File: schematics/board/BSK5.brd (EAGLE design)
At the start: 94 x 94 mm, 26 parts

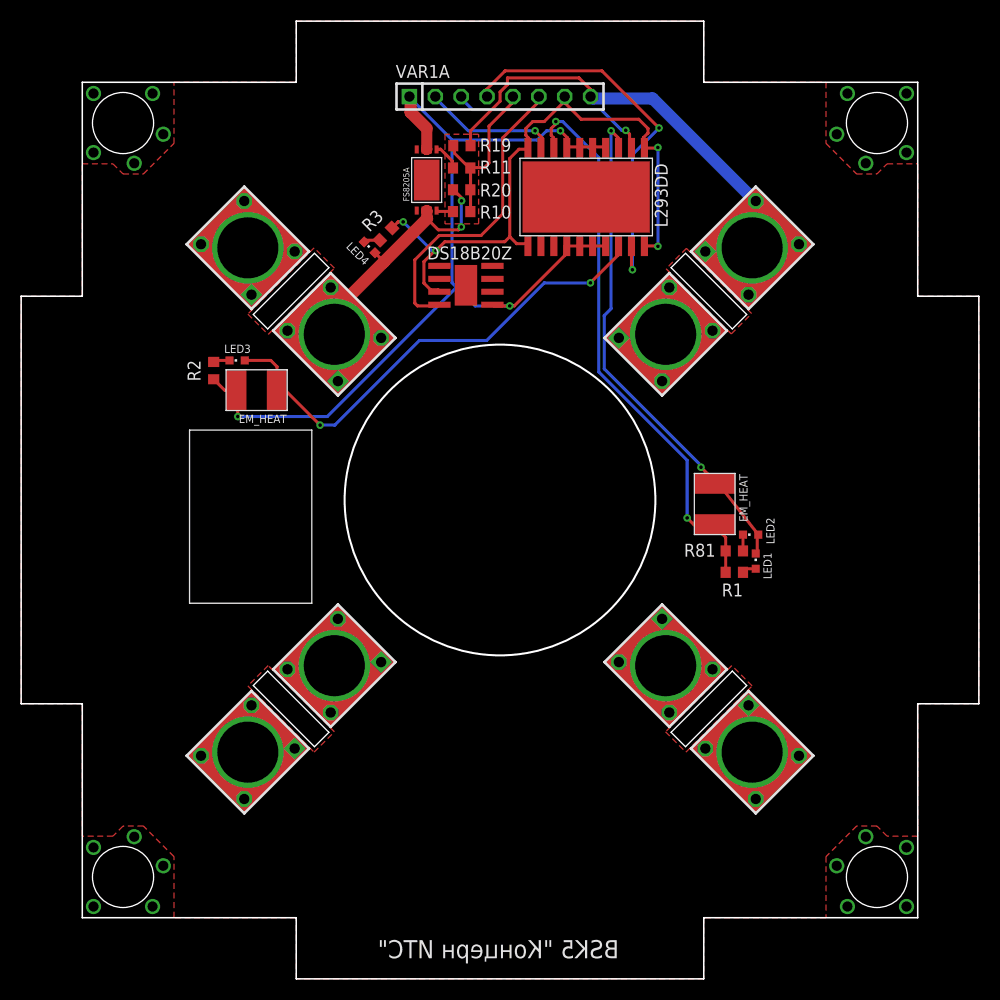
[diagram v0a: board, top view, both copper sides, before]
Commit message: Подписаны разъемы на платах
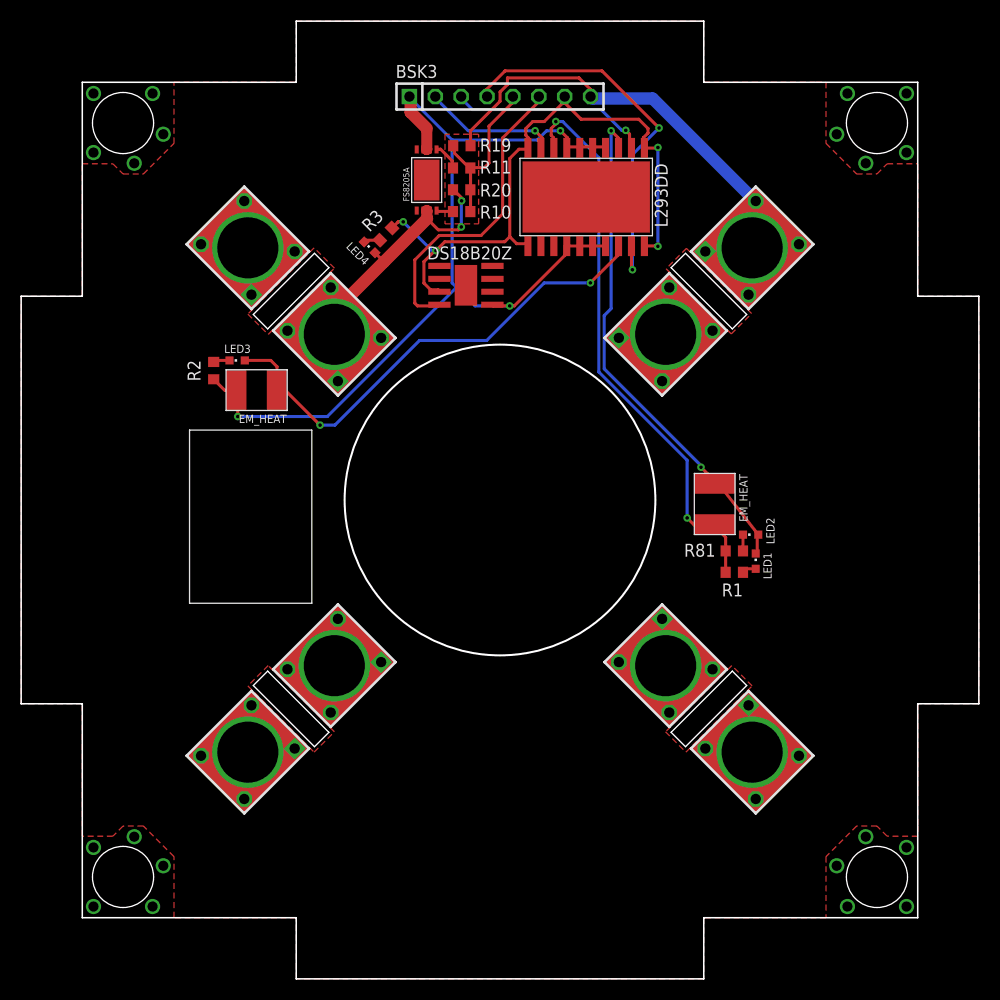
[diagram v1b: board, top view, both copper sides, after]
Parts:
- renumbered VAR1A to BSK3
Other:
- board text added: "to BSK3"
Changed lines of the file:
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@@
 <text x="58.3" y="28.7" size="1.4224" layer="26" rot="MR225">BUS-</text>
 <text x="32.2" y="25" size="1.4224" layer="26" rot="MR135">BUS-</text>
-<text x="35" y="3.8" size="1.778" layer="25" rot="MR180">BSK5 "Концерн ИТС"</text>
+<text x="35" y="3.8" size="1.778" layer="26" rot="MR180">BSK5 "Концерн ИТС"</text>
 <circle x="47" y="47" radius="15.25" width="0.2" layer="20"/>
+<text x="46.1" y="88.2" size="1.778" layer="26" rot="MR0">to BSK3</text>
 </plain>
 <attributes>
@@
 <attribute name="VALUE" x="29.311459375" y="24.30514375" size="1.27" layer="27" rot="R135"/>
 </element>
-<element name="VAR1A" library="pinheadCS" package="1X08" value="" x="47" y="86.6" smashed="yes">
+<element name="BSK3" library="pinheadCS" package="1X08" value="" x="47" y="86.6" smashed="yes">
 <attribute name="NAME" x="36.7638" y="88.4288" size="1.27" layer="25" ratio="10"/>
 <attribute name="VALUE" x="36.84" y="83.425" size="1.27" layer="27"/>
@@
 <contactref element="U$8" pad="17"/>
 <contactref element="U$14" pad="67"/>
-<contactref element="VAR1A" pad="1"/>
+<contactref element="BSK3" pad="1"/>
 <wire x1="54.7404" y1="71.9316" x2="53.6094" y2="71.9316" width="0.3" layer="1"/>
 <wire x1="53.6094" y1="71.9316" x2="53.555" y2="71.94" width="0.3" layer="1"/>
@@
 <contactref element="U$8" pad="11"/>
 <contactref element="U$8" pad="20"/>
-<contactref element="VAR1A" pad="7"/>
+<contactref element="BSK3" pad="7"/>
 <contactref element="U$5" pad="3"/>
 <wire x1="48.633" y1="72.1578" x2="49.5378" y2="72.1578" width="0.3" layer="1"/>
@@
 <signal name="1W">
 <contactref element="U$5" pad="4"/>
-<contactref element="VAR1A" pad="6"/>
+<contactref element="BSK3" pad="6"/>
 <wire x1="38.9064" y1="66.0504" x2="40.9422" y2="66.0504" width="0.3" layer="1"/>
 <wire x1="38.634" y1="66.3228" x2="38.9064" y2="66.0504" width="0.3" layer="1"/>
@@
 <signal name="BUS+">
 <contactref element="R19" pad="2"/>
-<contactref element="VAR1A" pad="8"/>
+<contactref element="BSK3" pad="8"/>
 <contactref element="U$3" pad="1"/>
 <contactref element="U$3" pad="2"/>
@@
 </signal>
 <signal name="KEM7">
-<contactref element="VAR1A" pad="3"/>
+<contactref element="BSK3" pad="3"/>
 <contactref element="U$8" pad="2"/>
 <wire x1="59.7168" y1="82.913" x2="59.7168" y2="81.6582" width="0.3" layer="1"/>
@@
 </signal>
 <signal name="KEM8">
-<contactref element="VAR1A" pad="2"/>
+<contactref element="BSK3" pad="2"/>
 <contactref element="U$8" pad="9"/>
 <wire x1="51.1212" y1="82.563" x2="51.1212" y2="81.6582" width="0.3" layer="1"/>
@@
 </signal>
 <signal name="KHEAT4">
-<contactref element="VAR1A" pad="4"/>
+<contactref element="BSK3" pad="4"/>
 <contactref element="U$8" pad="19"/>
 <wire x1="57.0024" y1="89.1228" x2="62.6126" y2="83.5126" width="0.3" layer="1"/>
@@
 </signal>
 <signal name="KVCC4">
-<contactref element="VAR1A" pad="5"/>
+<contactref element="BSK3" pad="5"/>
 <contactref element="R10" pad="1"/>
 <contactref element="R11" pad="1"/>

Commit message: Платы подготовлены для Резонита
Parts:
- removed U$14: FS8205A, CanCubeSat:FS8205A
- added FS8205A: FS8205A+, CanCubeSat:FS8205A+
- moved LED1 8.77 mm to (73.2, 49.7), turned to 90 degrees
- moved R1 8.52 mm to (73.2, 47.8)
- moved R3 4.84 mm to (38.2, 68.9), turned to 90 degrees
- moved R81 4.67 mm to (73.2, 45.4)
- moved LED3 3.89 mm to (18.5, 57.9), turned to 0 degrees
- moved LED4 3.70 mm to (36.5, 68.9), turned to 0 degrees
- moved R2 2.77 mm to (16.8, 57.9)
- moved LED2 1.60 mm to (73.2, 43.7), turned to 270 degrees
- renumbered U$5 to DS18B20, U$8 to L293DD
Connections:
- removed net HEAT: DS18B20.HEAT, L293DD.HEAT, U$14.HEAT
- net BUS-: now also FS8205A.23; no longer U$14.23
- net GND: now also DS18B20.HEAT, FS8205A.67, FS8205A.HEAT, L293DD.HEAT; no longer U$14.67
- net N$8: now also FS8205A.4; no longer U$14.4
- net N$9: now also FS8205A.5; no longer U$14.5
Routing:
- net GND: track 95.7 -> 148.5 mm, vias 3 -> 2
- net 5V: track 63.0 -> 58.4 mm, vias 4 -> 2
- net 1W: track 30.3 -> 34.9 mm
- net N$3: track 48.5 -> 51.9 mm
- net N$1: track 50.2 -> 53.0 mm
- net N$2: track 55.7 -> 57.5 mm
- net BUS-: track 45.3 -> 43.9 mm, vias 2 -> 0
- net N$27: track 1.39 -> 1.94 mm
- added copper zone on layer 1, net GND
- removed copper zone on layer 1, net HEAT
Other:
- board text added: "BUS"
- board text added: "EM+"
- board text added: "EM-"
- board text added: "HEATER"

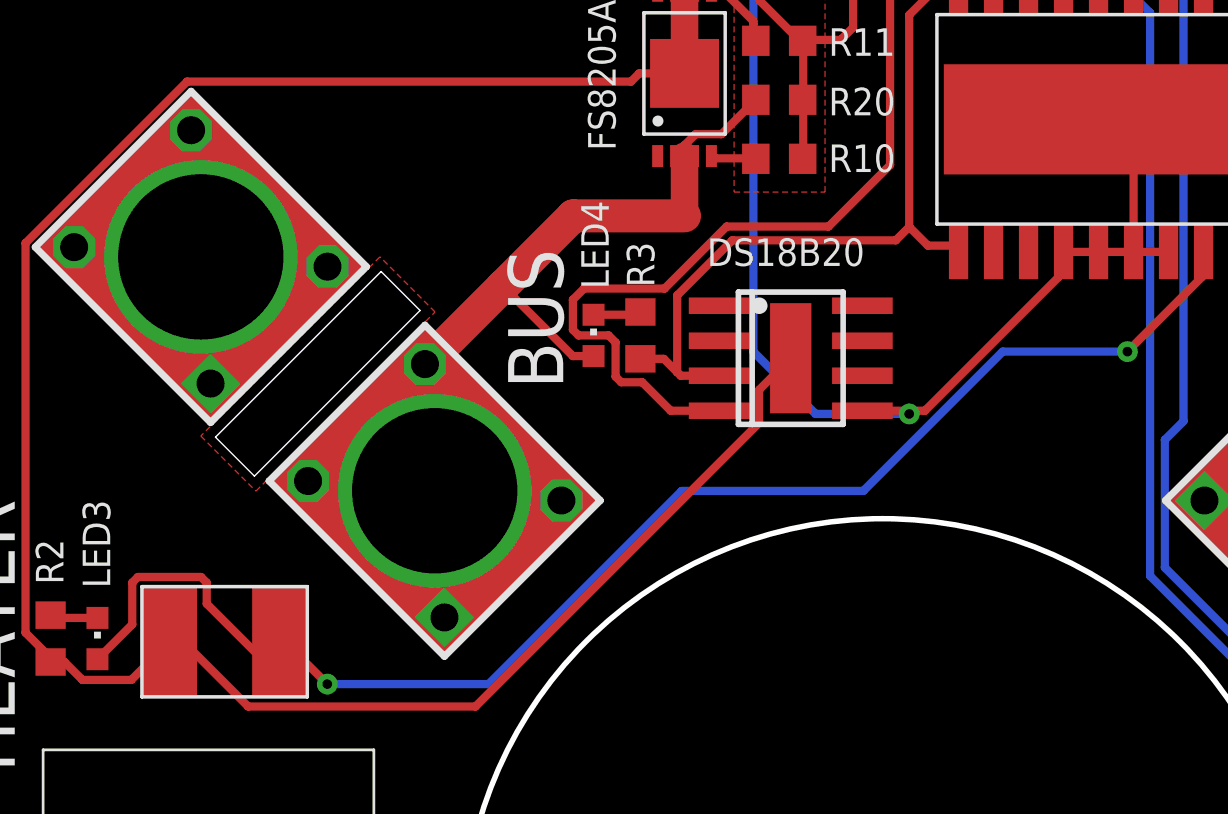
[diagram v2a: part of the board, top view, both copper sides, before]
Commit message: Исправлены RADIO и диоды
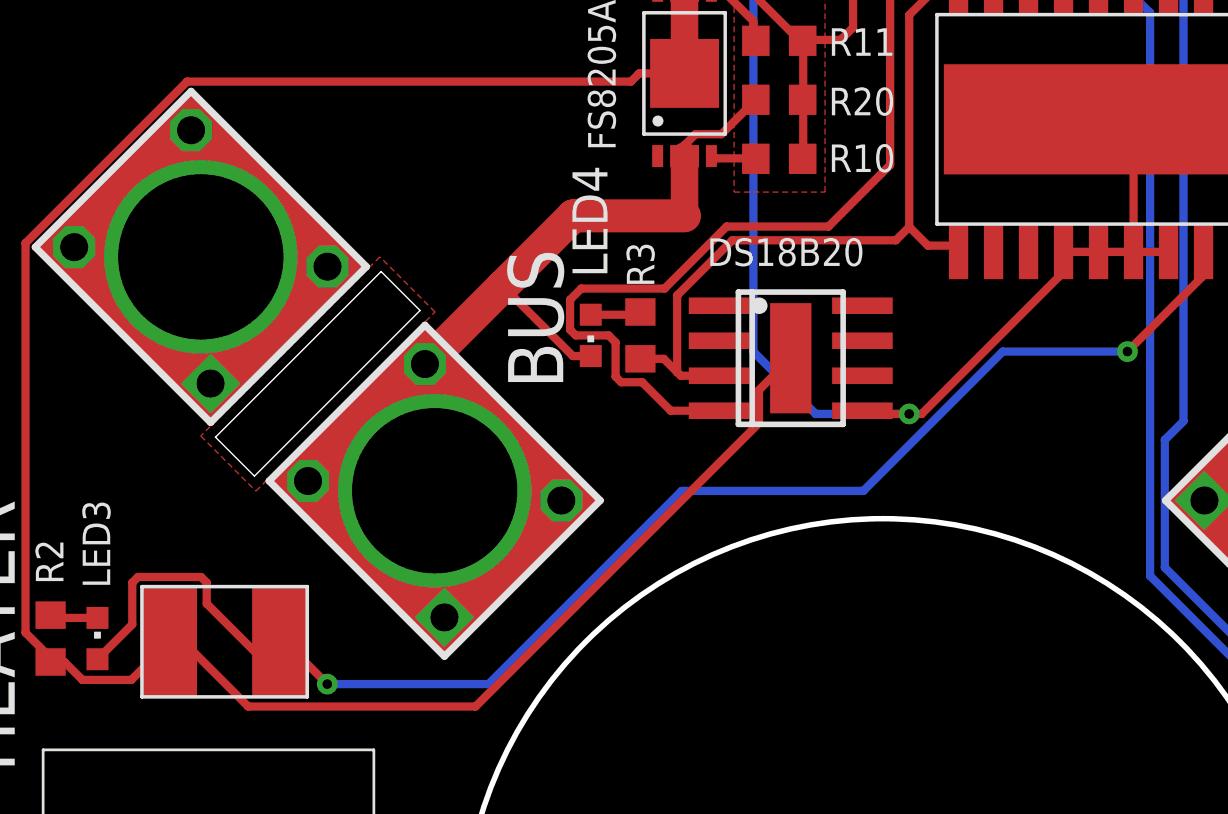
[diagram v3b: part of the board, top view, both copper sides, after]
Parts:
- moved LED4 0.10 mm to (36.4, 68.9), turned to 180 degrees
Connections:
- net BUS-: now also LED4.C; no longer LED4.A
- net N$29: now also LED4.A; no longer LED4.C
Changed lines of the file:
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@@
 <attribute name="VALUE" x="20.405" y="56.63" size="1.27" layer="27" rot="R90"/>
-</element>
-<element name="LED4" library="led" library_urn="urn:adsk.eagle:library:259" package="CHIPLED_0603" package3d_urn="urn:adsk.eagle:package:15822/2" value="" x="36.5" y="68.9" smashed="yes">
-<attribute name="NAME" x="37.052865625" y="70.583553125" size="1" layer="25" rot="R90"/>
-<attribute name="POPULARITY" value="28" x="31.599996875" y="74.400003125" size="1.778" layer="27" display="off"/>
-<attribute name="VALUE" x="38.404996875" y="67.630003125" size="1.27" layer="27" rot="R90"/>
 </element>
 <element name="R3" library="resistor" library_urn="urn:adsk.eagle:library:348" package="R0603" package3d_urn="urn:adsk.eagle:package:23555/3" value="2k" x="38.2" y="68.9" smashed="yes" rot="R90">
 <attribute name="NAME" x="38.707640625" y="70.6478375" size="1" layer="25" rot="R90"/>
 <attribute name="VALUE" x="40.104996875" y="68.265" size="1.27" layer="27" rot="R90"/>
+</element>
+<element name="LED4" library="led" library_urn="urn:adsk.eagle:library:259" package="CHIPLED_0603" package3d_urn="urn:adsk.eagle:package:15822/2" value="" x="36.4" y="68.9" smashed="yes" rot="R180">
+<attribute name="NAME" x="35.735" y="75.07" size="1.27" layer="25" rot="R270"/>
+<attribute name="POPULARITY" value="28" x="41.3" y="63.3" size="1.778" layer="27" rot="R180" display="off"/>
+<attribute name="VALUE" x="34.495" y="70.17" size="1.27" layer="27" rot="R270"/>
 </element>
 </elements>
@@
 <wire x1="38.2278" y1="86.4084" x2="38.11" y2="86.6" width="0.3" layer="16"/>
 <wire x1="42.2994" y1="82.3368" x2="42.2994" y2="68.3124" width="0.3" layer="16"/>
-<wire x1="21.2628" y1="57.681" x2="21.114" y2="57.785" width="0.3" layer="1"/>
 <wire x1="44.5614" y1="66.0504" x2="47.9544" y2="66.0504" width="0.3" layer="16"/>
 <wire x1="42.2994" y1="68.3124" x2="44.5614" y2="66.0504" width="0.3" layer="16"/>
@@
 <wire x1="56.095" y1="71.94" x2="56.095" y2="76.105" width="0.3" layer="1"/>
 <wire x1="56.095" y1="76.105" x2="55.46" y2="76.74" width="0.3" layer="1"/>
-<wire x1="48.5234" y1="66.167" x2="46.256" y2="66.167" width="0.3" layer="1"/>
-<wire x1="53.3832" y1="71.0268" x2="48.5234" y2="66.167" width="0.3" layer="1"/>
 <wire x1="17.305025" y1="57.05" x2="16.8" y2="57.05" width="0.3" layer="1"/>
 <wire x1="17.955025" y1="56.4" x2="17.305025" y2="57.05" width="0.3" layer="1"/>
@@
 <wire x1="23.969025" y1="55.435" x2="32.218975" y2="55.435" width="0.3" layer="1"/>
 <wire x1="32.218975" y1="55.435" x2="42.506" y2="65.722025" width="0.3" layer="1"/>
+<wire x1="48.4068" y1="66.0504" x2="47.9544" y2="66.0504" width="0.3" layer="1"/>
+<wire x1="53.3832" y1="71.0268" x2="48.4068" y2="66.0504" width="0.3" layer="1"/>
+<wire x1="47.9544" y1="66.0504" x2="46.3726" y2="66.0504" width="0.3" layer="1"/>
+<wire x1="46.3726" y1="66.0504" x2="46.256" y2="66.167" width="0.3" layer="1"/>
 </signal>
 <signal name="5V">
@@
 <wire x1="50.81" y1="86.0972" x2="47.262" y2="82.5492" width="0.3" layer="1"/>
 <wire x1="37.505025" y1="67.2" x2="37.3" y2="67.405025" width="0.3" layer="1"/>
-<wire x1="37.044975" y1="68.9" x2="35.955025" y2="68.9" width="0.3" layer="1"/>
-<wire x1="35.955025" y1="68.9" x2="35.75" y2="69.105025" width="0.3" layer="1"/>
-<wire x1="35.75" y1="69.105025" x2="35.75" y2="70.194975" width="0.3" layer="1"/>
+<wire x1="37.044975" y1="68.9" x2="35.855025" y2="68.9" width="0.3" layer="1"/>
+<wire x1="35.855025" y1="68.9" x2="35.65" y2="69.105025" width="0.3" layer="1"/>
+<wire x1="35.65" y1="69.105025" x2="35.65" y2="70.194975" width="0.3" layer="1"/>
 <wire x1="41.3271125" y1="72.8502" x2="45.0276" y2="72.8502" width="0.3" layer="1"/>
 <wire x1="39.0769125" y1="70.6" x2="41.3271125" y2="72.8502" width="0.3" layer="1"/>
@@
 <wire x1="37.3" y1="67.405025" x2="37.3" y2="68.644975" width="0.3" layer="1"/>
 <wire x1="37.3" y1="68.644975" x2="37.044975" y2="68.9" width="0.3" layer="1"/>
-<wire x1="35.75" y1="70.194975" x2="36.155025" y2="70.6" width="0.3" layer="1"/>
-<wire x1="36.155025" y1="70.6" x2="39.0769125" y2="70.6" width="0.3" layer="1"/>
+<wire x1="35.65" y1="70.194975" x2="36.055025" y2="70.6" width="0.3" layer="1"/>
+<wire x1="36.055025" y1="70.6" x2="39.0769125" y2="70.6" width="0.3" layer="1"/>
 <wire x1="45.0276" y1="72.8502" x2="47.262" y2="75.0846" width="0.3" layer="1"/>
 </signal>
@@
 <wire x1="30.3108" y1="63.5622" x2="30.737" y2="63.263" width="0.3" layer="1"/>
 <wire x1="30.3108" y1="66.2766" x2="30.737" y2="63.263" width="0.3" layer="1"/>
-<contactref element="LED4" pad="A"/>
 <wire x1="39.802" y1="75.406" x2="39.802" y2="75.802" width="0.3" layer="1"/>
 <wire x1="39.802" y1="75.802" x2="40.2" y2="76.2" width="0.3" layer="1"/>
@@
 <wire x1="39.802" y1="73.237875" x2="35.762125" y2="73.237875" width="1.2" layer="1"/>
 <wire x1="39.802" y1="75.406" x2="39.802" y2="73.237875" width="1" layer="1"/>
-<wire x1="36.5" y1="68.15" x2="35.75" y2="68.15" width="0.3" layer="1"/>
-<wire x1="35.75" y1="68.15" x2="33.212125" y2="70.687875" width="0.3" layer="1"/>
+<wire x1="33.212125" y1="70.687875" x2="35.75" y2="68.15" width="0.3" layer="1"/>
+<contactref element="LED4" pad="C"/>
+<wire x1="35.75" y1="68.15" x2="36.4" y2="68.15" width="0.3" layer="1"/>
 </signal>
 <signal name="N$8">
@@
 </signal>
 <signal name="N$29">
-<contactref element="LED4" pad="C"/>
+<contactref element="LED4" pad="A"/>
 <contactref element="R3" pad="2"/>
-<wire x1="36.5" y1="69.65" x2="38.1" y2="69.65" width="0.3" layer="1"/>
+<wire x1="36.4" y1="69.65" x2="38.1" y2="69.65" width="0.3" layer="1"/>
 <wire x1="38.1" y1="69.65" x2="38.2" y2="69.75" width="0.3" layer="1"/>
 </signal>

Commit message: Резисторы у FS8205A 100Ом
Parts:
- R10, R11: value 10k -> 100R
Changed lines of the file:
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@@
 </autorouter>
 <elements>
-<element name="R10" library="resistor" library_urn="urn:adsk.eagle:library:348" package="R0603" package3d_urn="urn:adsk.eagle:package:23555/3" value="10k" x="43.239" y="75.308" smashed="yes" rot="R180">
+<element name="R10" library="resistor" library_urn="urn:adsk.eagle:library:348" package="R0603" package3d_urn="urn:adsk.eagle:package:23555/3" value="100R" x="43.239" y="75.308" smashed="yes" rot="R180">
 <attribute name="NAME" x="45.026" y="74.827" size="1" layer="25"/>
 <attribute name="VALUE" x="43.874" y="77.213" size="1.27" layer="27" rot="R180"/>
 </element>
-<element name="R11" library="resistor" library_urn="urn:adsk.eagle:library:348" package="R0603" package3d_urn="urn:adsk.eagle:package:23555/3" value="10k" x="43.239" y="79.59" smashed="yes" rot="R180">
+<element name="R11" library="resistor" library_urn="urn:adsk.eagle:library:348" package="R0603" package3d_urn="urn:adsk.eagle:package:23555/3" value="100R" x="43.239" y="79.59" smashed="yes" rot="R180">
 <attribute name="NAME" x="45.026" y="79.045" size="1" layer="25"/>
 <attribute name="VALUE" x="43.874" y="81.495" size="1.27" layer="27" rot="R180"/>

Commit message: Добавлены новые диоды
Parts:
- added LAP4: LAP4-BOTTOM, led:P47F-BOTTOM
- moved LED4 0.71 mm to (35.7, 68.8)
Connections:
- net BUS-: now also LAP4.C
- net N$29: now also LAP4.A
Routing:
- net N$29: track 1.84 -> 69.1 mm, vias 0 -> 4
- net BUS-: track 43.8 -> 90.4 mm, vias 0 -> 2
- net 1W: track 35.1 -> 36.3 mm
- net GND: track 148.4 -> 149.3 mm
